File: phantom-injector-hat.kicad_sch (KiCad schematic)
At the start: 41 parts, among them J1 Conn_02x20_Odd_Even, J2 Conn_02x03_Top_Bottom, J3 Conn_01x03, J4 Conn_01x03, SW1 SW_SPST, SW2 SW_SPST, U1 LT8362EMSE-PBF

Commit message: Fix C12 footprint: 4.7pF FBX feedforward cap is 0805, not 1812
Co-Authored-By: Claude Sonnet 4.6 <noreply@anthropic.com>
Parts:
- C12: footprint Capacitor_SMD:C_1812_4532Metric_Pad1.57x3.40mm_HandSolder -> Capacitor_SMD:C_0805_2012Metric_Pad1.18x1.45mm_HandSolder

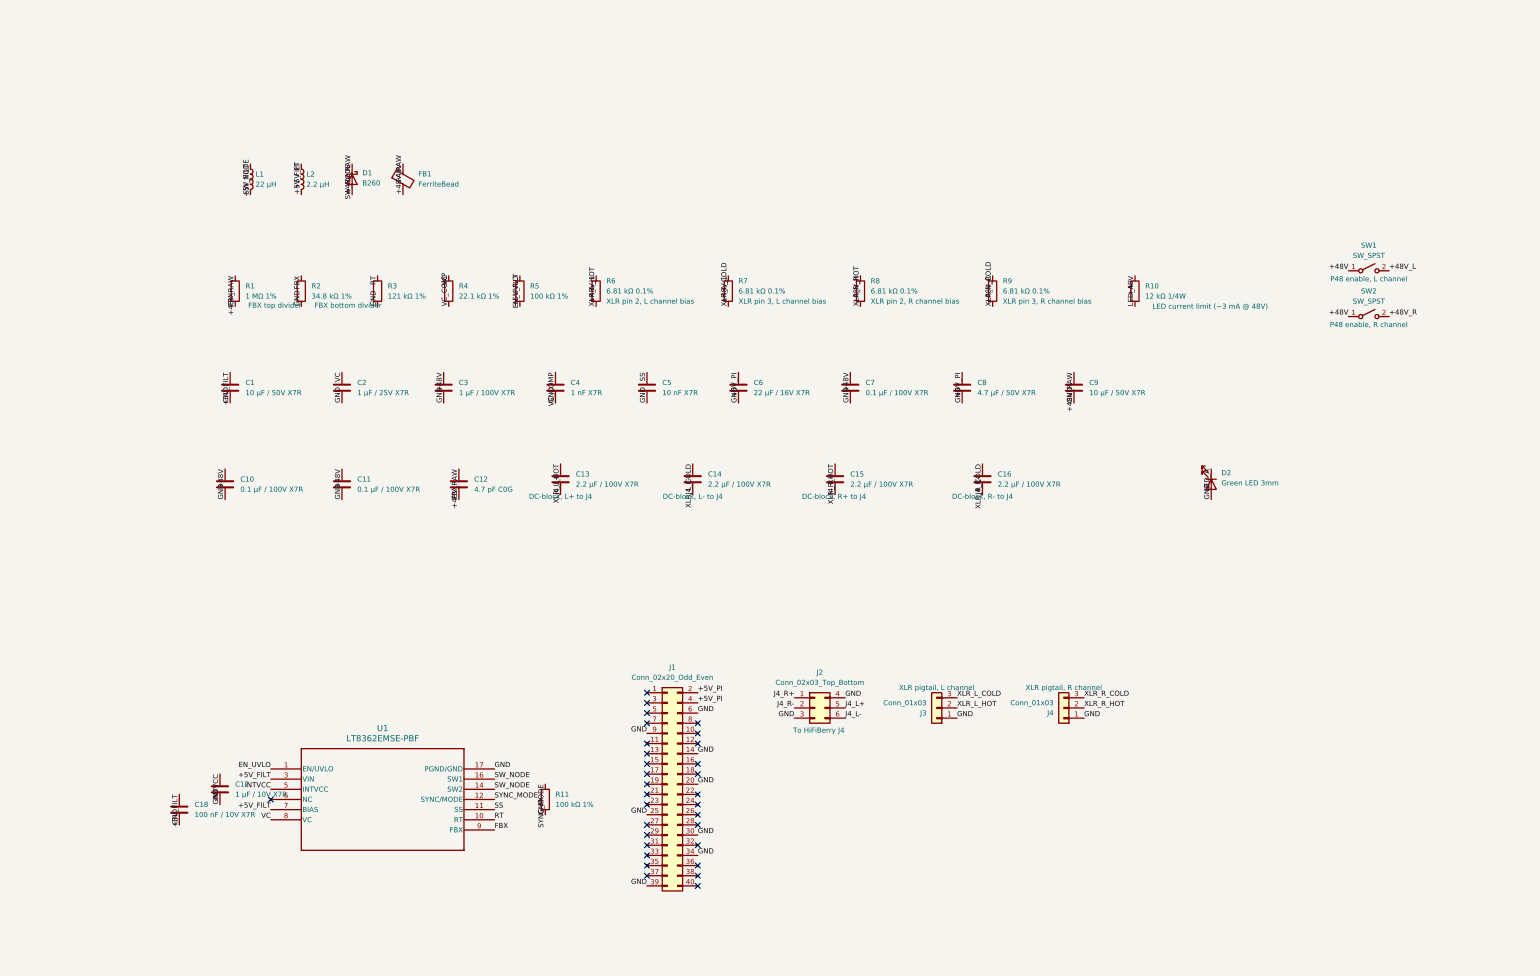
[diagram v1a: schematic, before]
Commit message: Downsize footprints to 0805 for hot-plate reflow; fix component placement overlaps
- C1, C3, C6, C8, C13-C16: 1210/1206/1812 → 0805 (C9 stays 1206, on 48V rail)
- FB1: 1206 → 0805 ferrite bead
- place_components.py: fix overlapping groups (R6-R9 spacing, C13-C16 two-column
  layout, C10/FB1 vertical clearance, R10/D2 moved below J1 courtyard, J3/J4
  repositioned away from R2)

Co-Authored-By: Claude Sonnet 4.6 <noreply@anthropic.com>
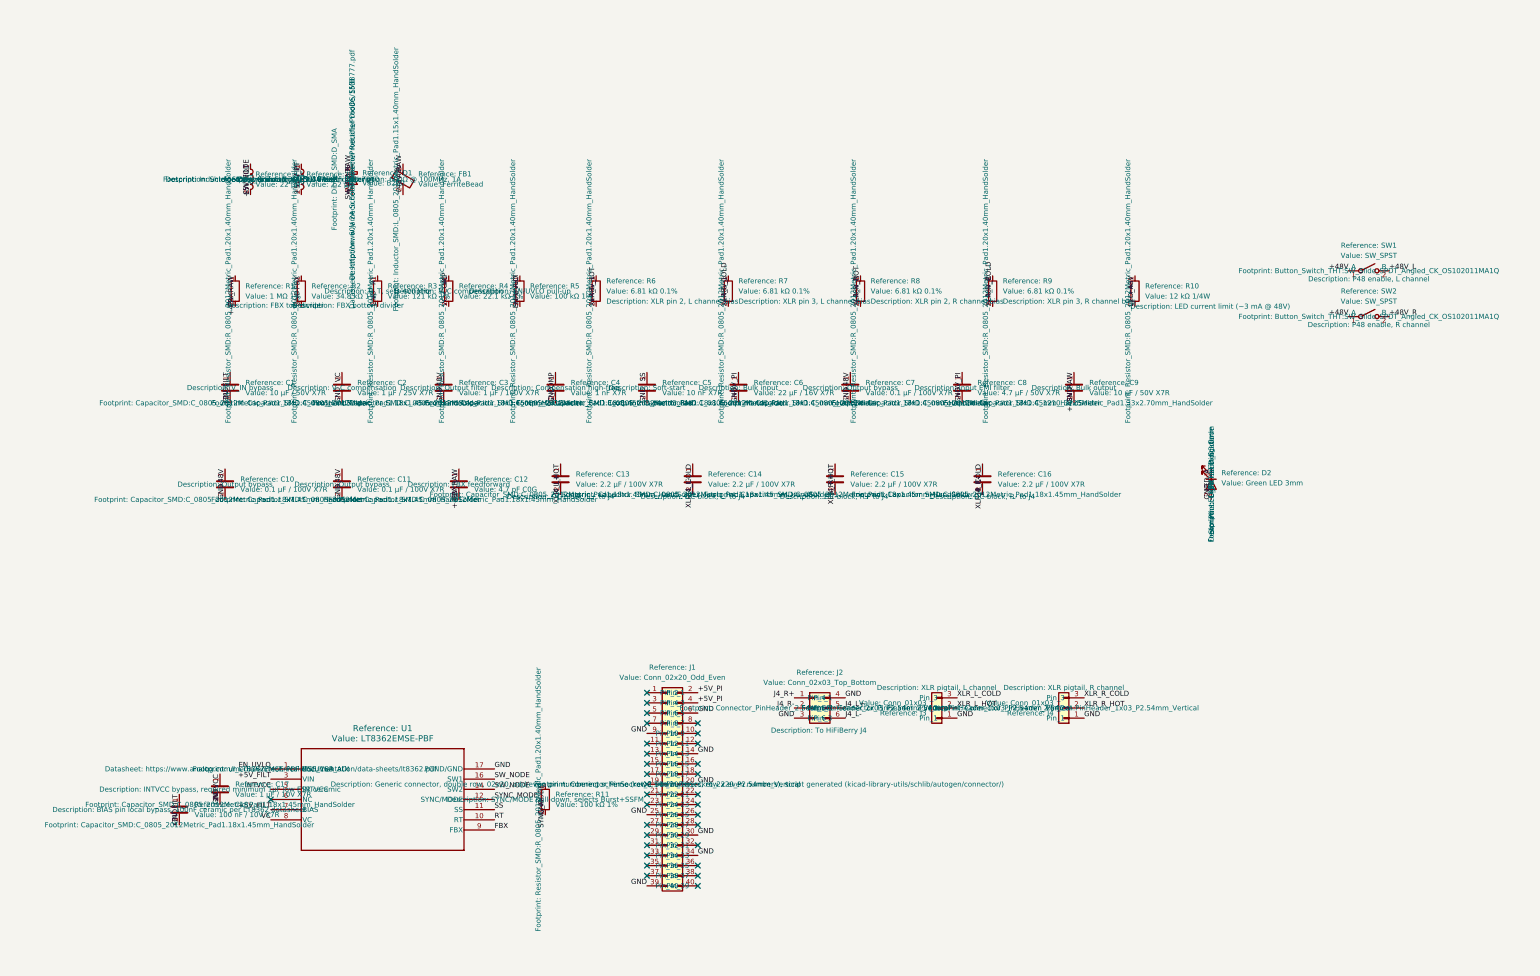
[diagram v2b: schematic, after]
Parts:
- C1, C6, C8: footprint Capacitor_SMD:C_1210_3225Metric_Pad1.33x2.70mm_HandSolder -> Capacitor_SMD:C_0805_2012Metric_Pad1.18x1.45mm_HandSolder
- C13, C14, C15, C16: footprint Capacitor_SMD:C_1812_4532Metric_Pad1.57x3.40mm_HandSolder -> Capacitor_SMD:C_0805_2012Metric_Pad1.18x1.45mm_HandSolder
- C3: footprint Capacitor_SMD:C_1206_3216Metric_Pad1.33x1.80mm_HandSolder -> Capacitor_SMD:C_0805_2012Metric_Pad1.18x1.45mm_HandSolder
- FB1: footprint Inductor_SMD:L_1206_3216Metric_Pad1.22x1.90mm_HandSolder -> Inductor_SMD:L_0805_2012Metric_Pad1.15x1.40mm_HandSolder
